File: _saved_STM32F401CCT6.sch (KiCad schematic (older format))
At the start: 42 parts, among them J1 USB_OTG, J2 Conn_02x03_Odd_Even, J3 Conn_01x20_des, J4 Conn_01x05_desc, J5 Conn_01x20, SW1 SW_Push, U1 MIC5219-3.3, U2 STM32F401CCT6, U3 USBLC6-2SC6, Y1 32.786K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

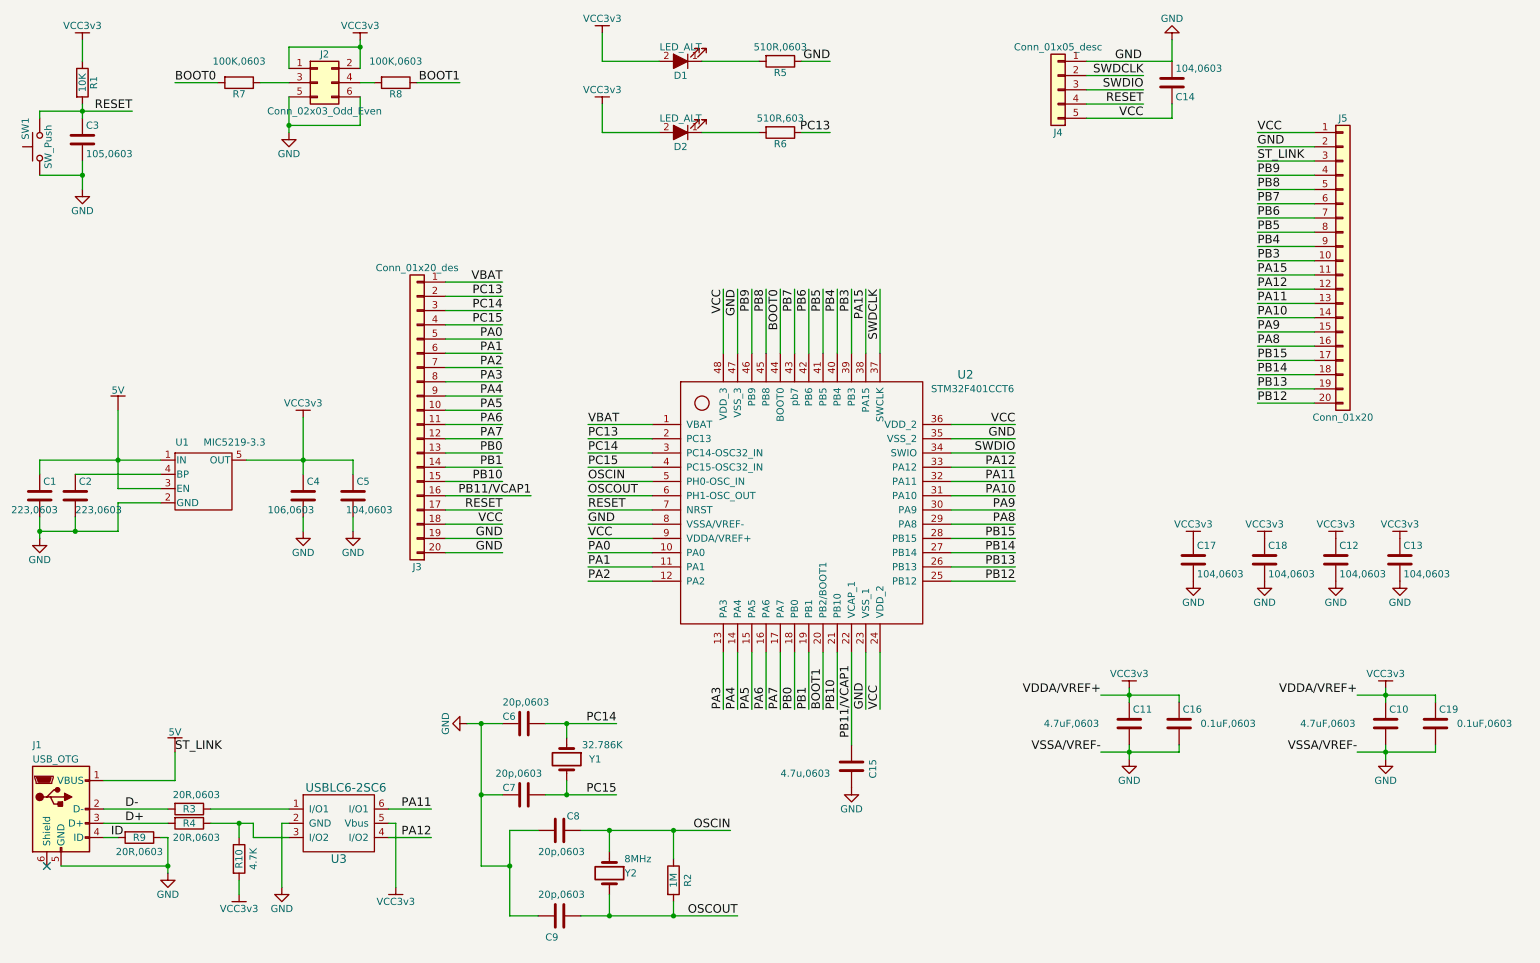
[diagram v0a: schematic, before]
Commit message: Change pin20 to Pwr Enable and added a resistor on it
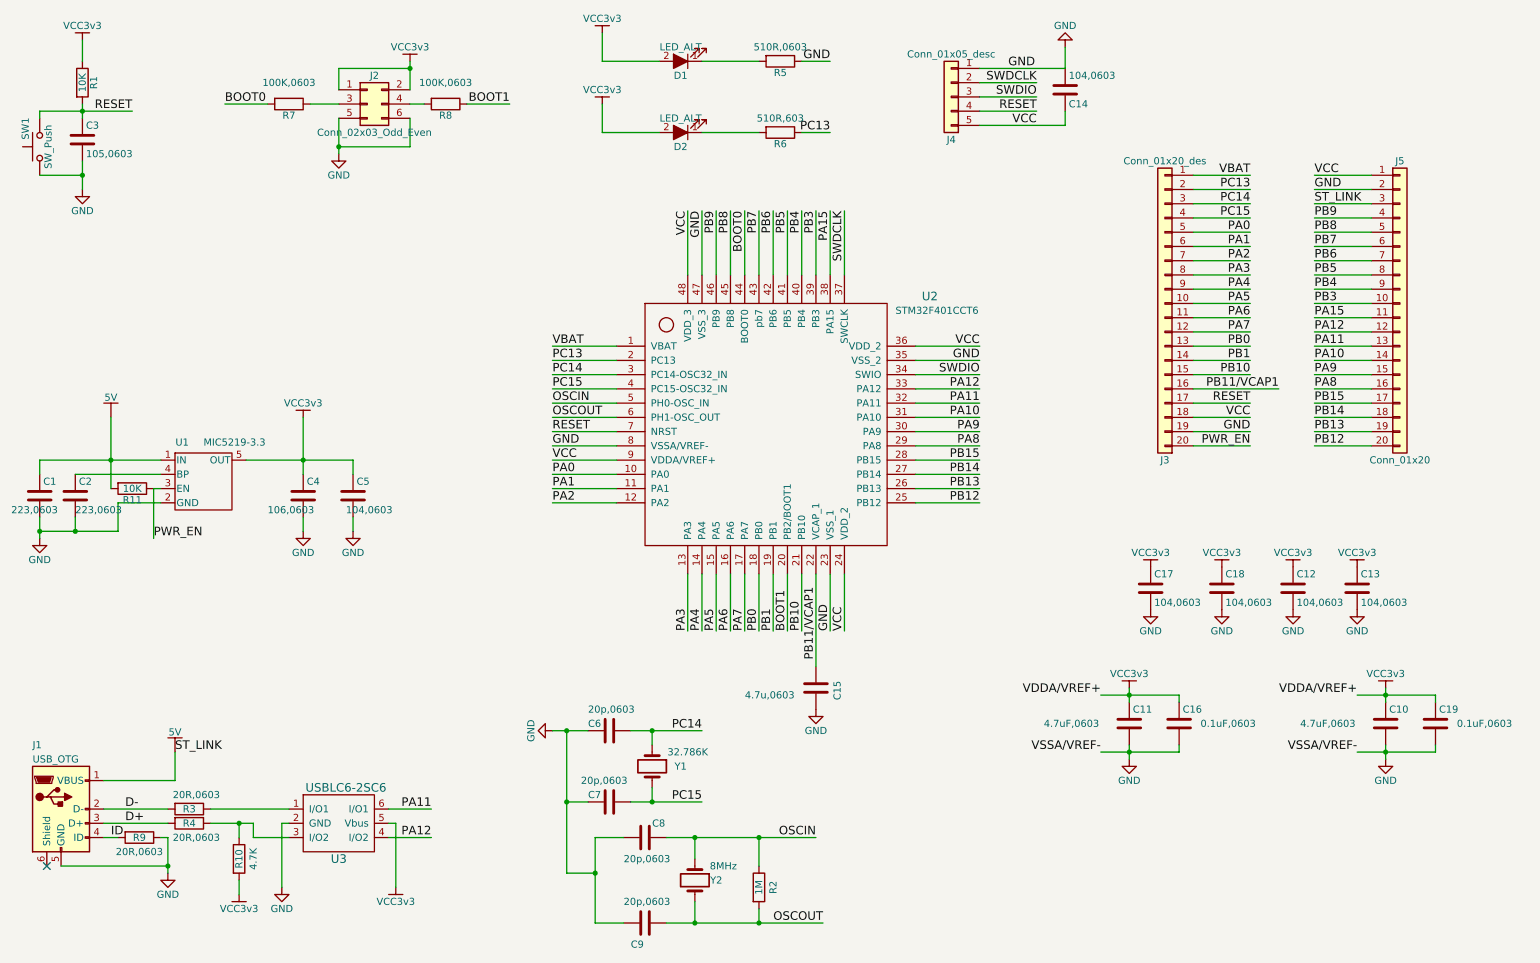
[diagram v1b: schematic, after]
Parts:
- added R11: 10K, Resistors_SMD:R_0603, symbol R
- U2: footprint (none) -> QFPN48:QFN_QFP48
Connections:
- net +5V: now also R11.2; no longer U1.3 (EN)
- net GND: no longer J3.20 (Pin_20)
- new net PWR_EN: J3.20 (Pin_20), R11.1, U1.3 (EN)
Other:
- moved on the sheet: C12, C13, C14, C15, C17, C18, C6, C7, C8, C9, J2, J3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
